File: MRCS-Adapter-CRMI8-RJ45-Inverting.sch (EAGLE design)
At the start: 4 parts

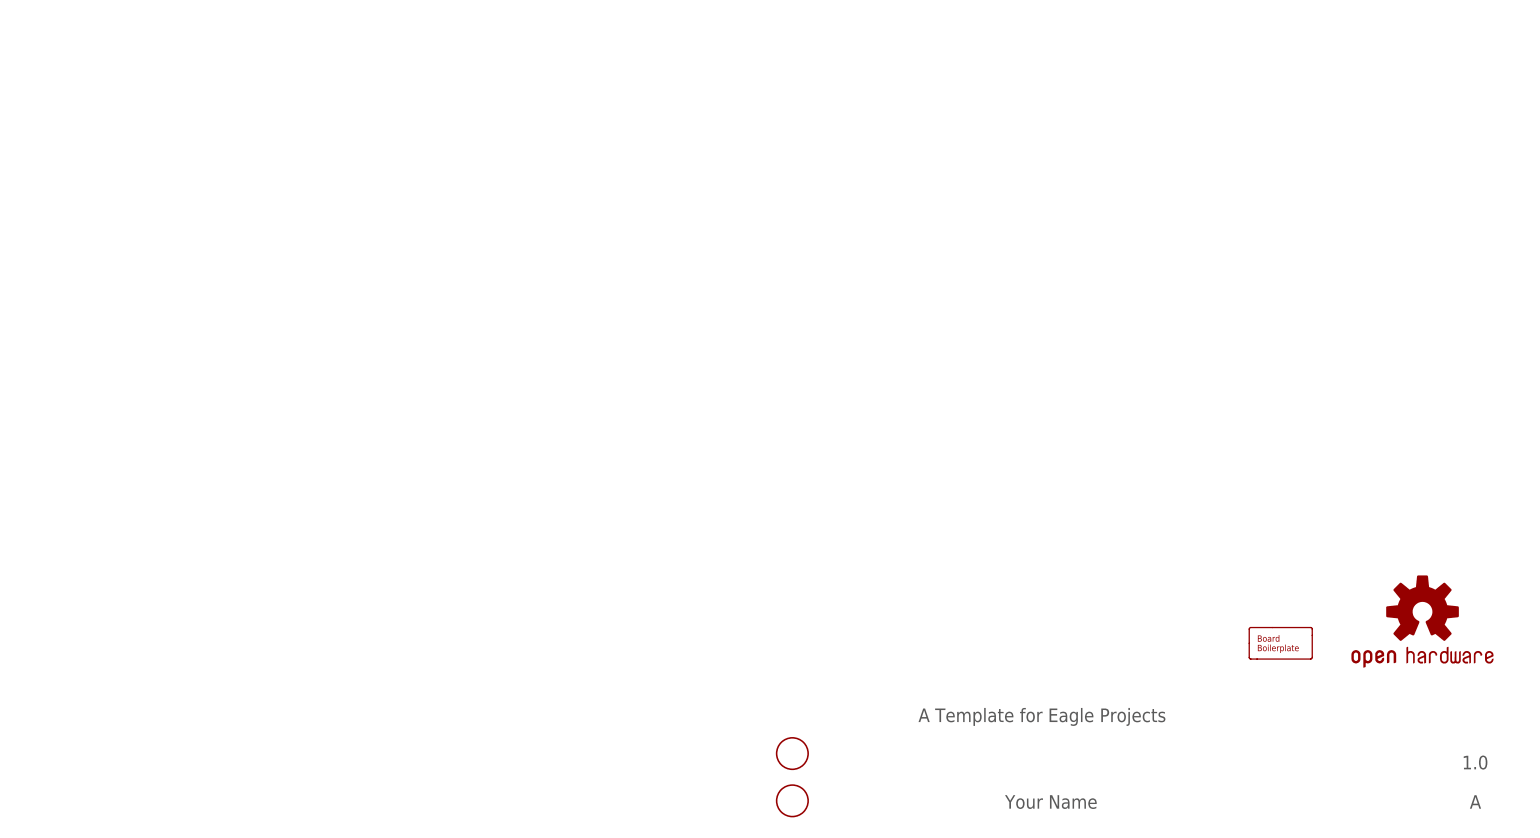
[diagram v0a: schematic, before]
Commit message: upload starting copy from non-inverting design
starting from older design
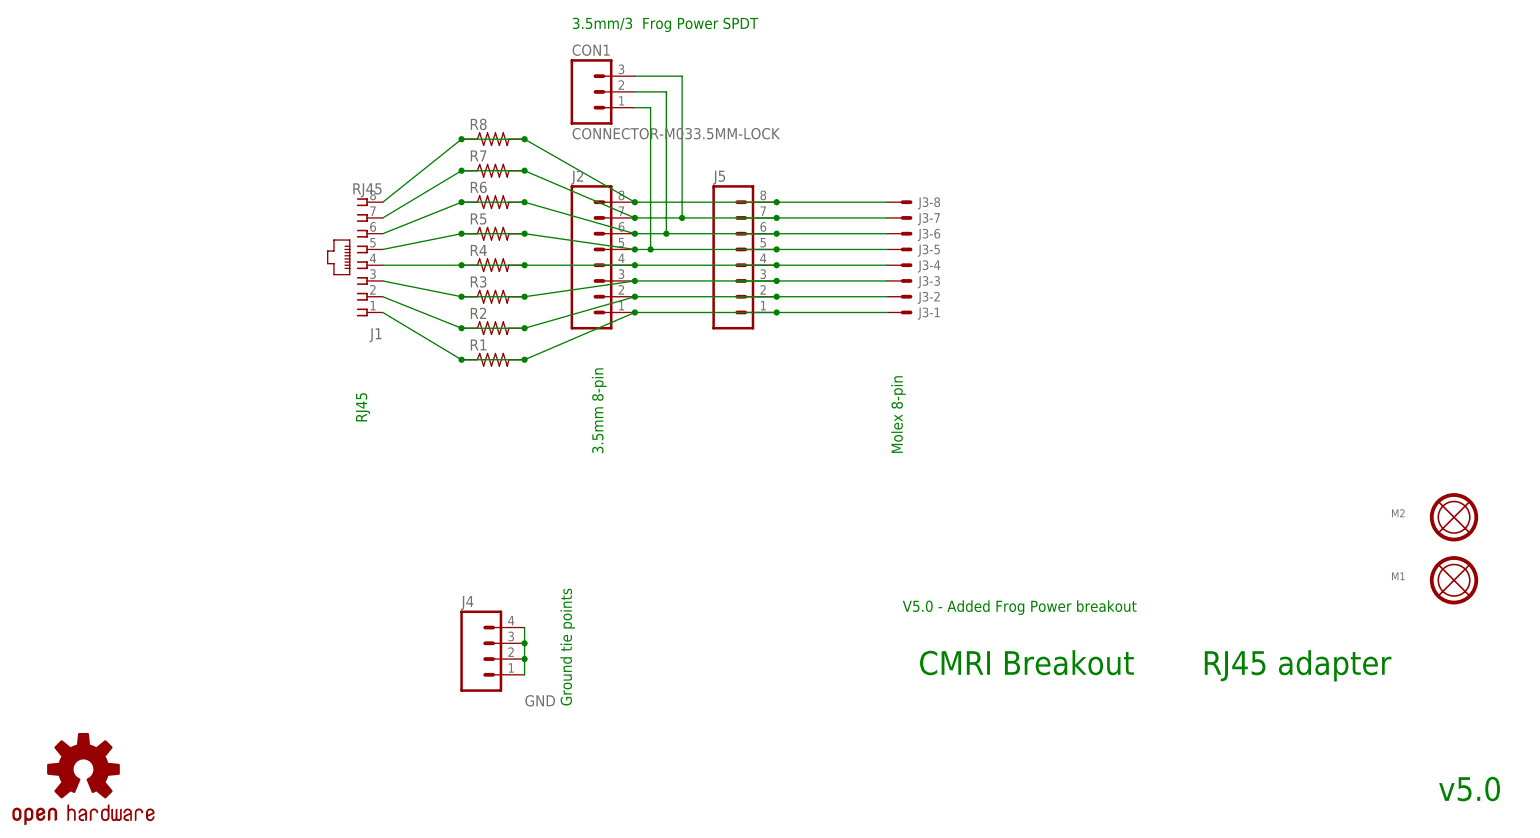
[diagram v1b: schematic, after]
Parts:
- removed BOARD1: BOARD80X100, SPCoast:BOARD80X100
- removed FID1, FID2: FIDUCIAL, SPCoast:FIDUCIAL
- removed OSHW1: DOC-OSHW-LOGO-M, SPCoast:DOC-OSHW-LOGO-M
- added CON1: CONNECTOR-M033.5MM-LOCK, SPCoast:CONNECTOR-M033.5MM-LOCK
- added J1: RJ45, SPCoast:CONNECTOR-RJ45-FRONT
- added J2: (no value), SPCoast:CONNECTOR-M083.5MM-8
- added J3: (no value), SPCoast:KK-156-8F
- added J4: (no value), SPCoast:CONNECTOR-M04SCREW_LOCK
- added J5: (no value), SPCoast:CONNECTOR-M08LOCK
- added M1, M2: MOUNTINGHOLE, SPCoast:MOUNTINGHOLE
- added R1, R2, R3, R4, R5, R6, R7, R8: (no value), SPCoast:RPTH04
- added U$1: DOC-OSHW-LOGO-L, SPCoast:DOC-OSHW-LOGO-L
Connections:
- new net GND: J4.1, J4.2, J4.3, J4.4
- new net L1: J1.1, J2.1, J3-1.S, J5.1, R1.1, R1.2
- new net L2: J1.2, J2.2, J3-2.S, J5.2, R2.1, R2.2
- new net L3: J1.3, J2.3, J3-3.S, J5.3, R3.1, R3.2
- new net L4: J1.4, J2.4, J3-4.S, J5.4, R4.1, R4.2
- new net L5: CON1.1, J1.5, J2.5, J3-5.S, J5.5, R5.1, R5.2
- new net L6: CON1.2, J1.6, J2.6, J3-6.S, J5.6, R6.1, R6.2
- new net L7: CON1.3, J1.7, J2.7, J3-7.S, J5.7, R7.1, R7.2
- new net L8: J1.8, J2.8, J3-8.S, J5.8, R8.1, R8.2
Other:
- note added: "3.5mm 8-pin"
- note added: "3.5mm/3 Frog Power SPDT"
- note added: "CMRI Breakout"
- note added: "Ground tie points"
- note added: "Molex 8-pin"
- note added: "RJ45"
- note added: "RJ45 adapter"
- note added: "V5.0 - Added Frog Power breakout"
- note added: "v5.0"
- note removed: "1.0"
- note removed: "A"
- note removed: "A Template for Eagle Projects"
- note removed: "Your Name"
